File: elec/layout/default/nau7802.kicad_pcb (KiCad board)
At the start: 2 copper layers, 225.7 x 100.8 mm, 7 parts

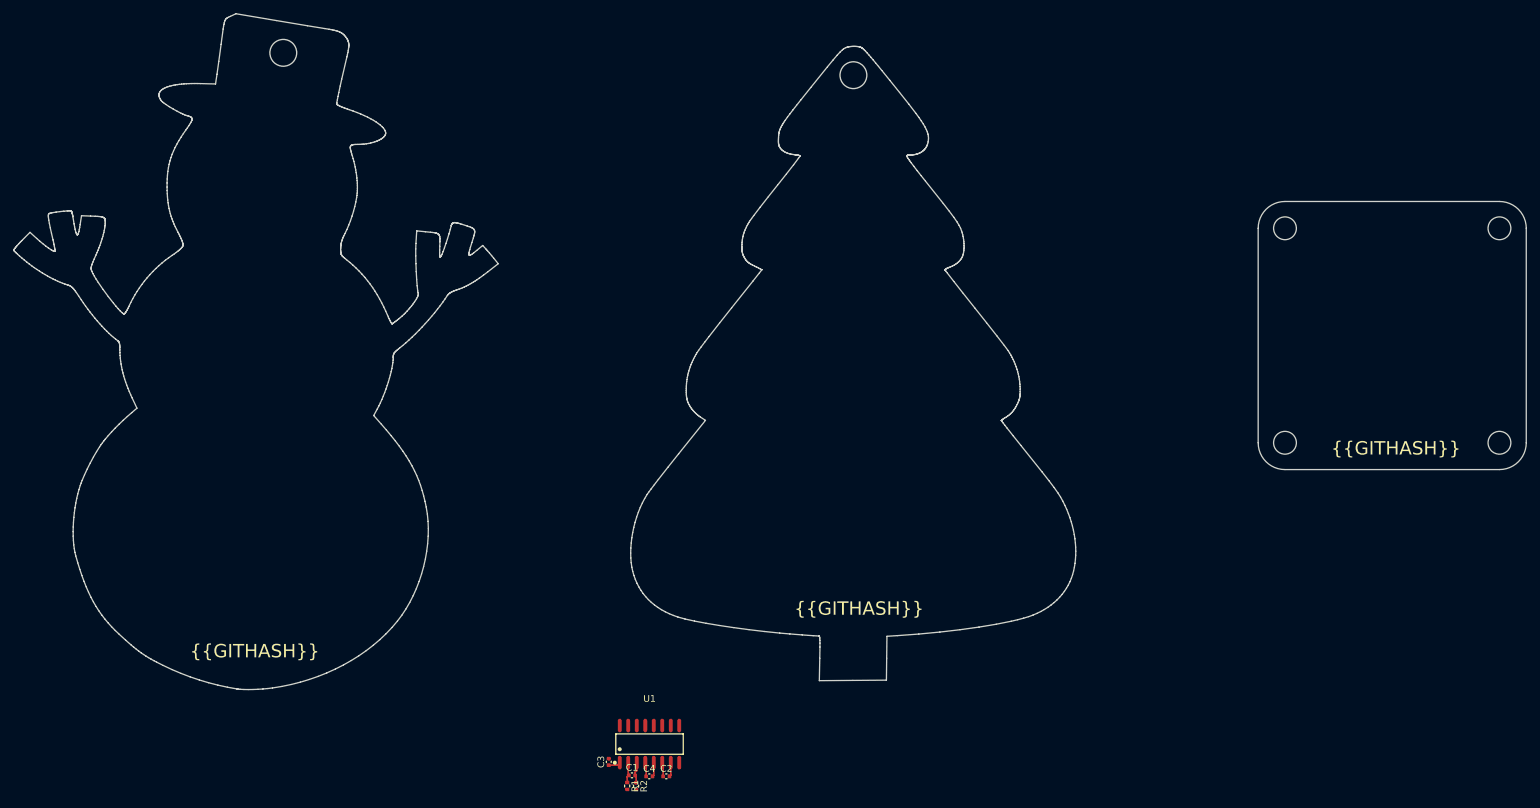
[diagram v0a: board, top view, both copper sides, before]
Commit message: Add dual sensor build
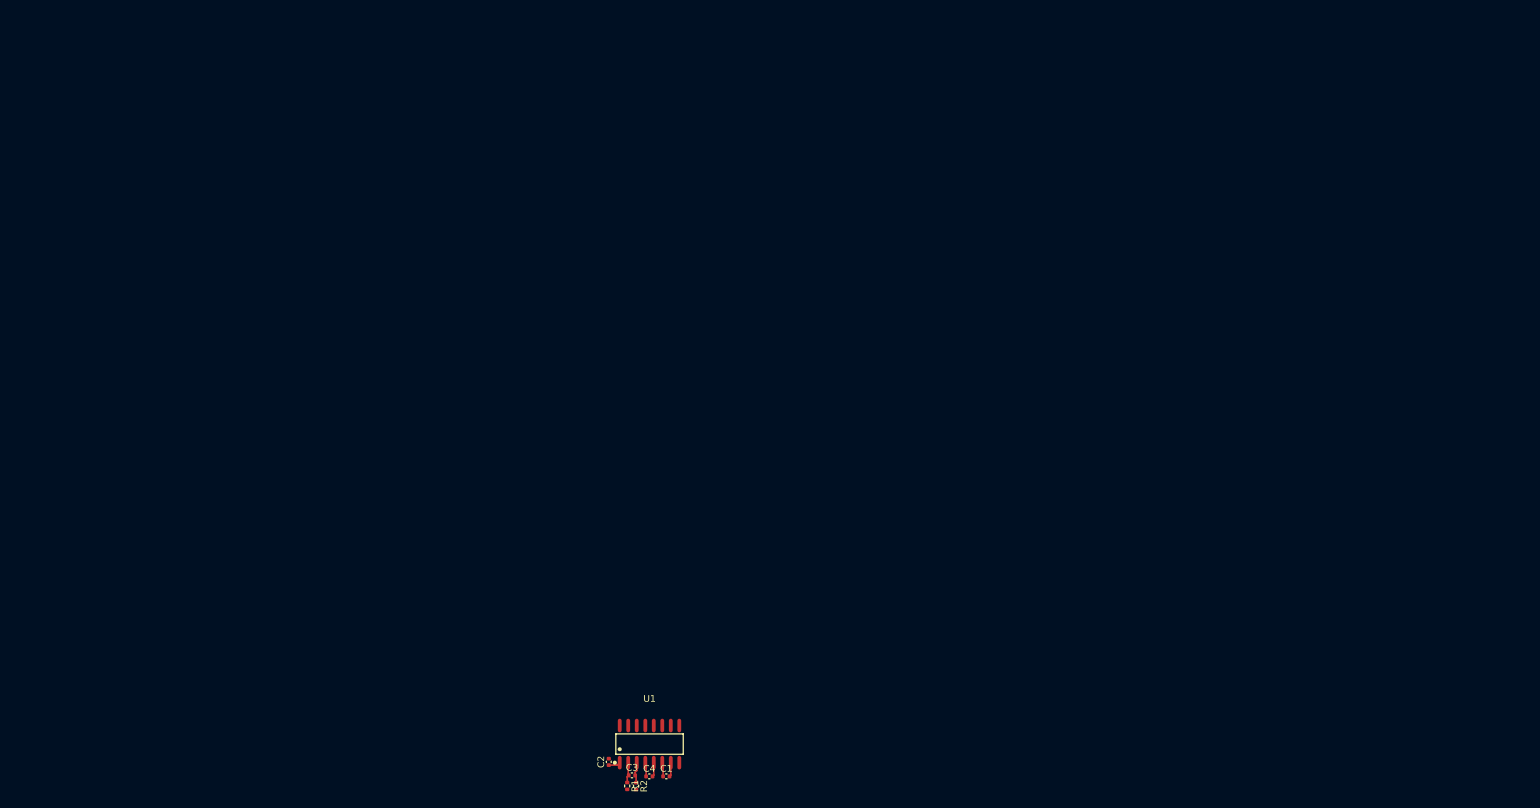
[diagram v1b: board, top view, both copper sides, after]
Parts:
- C1: renamed from C2; value Multilayer Ceramic Capacitors MLCC - SMD/SMT 100nF 10V 0402 RoHS -> 16V 100nF X7R ±10% 0402 Multilayer Ceramic Capacitors MLCC - SMD/SMT ROHS
- C2: renamed from C3; value Multilayer Ceramic Capacitors MLCC - SMD/SMT 100nF 10V 0402 RoHS -> 16V 100nF X7R ±10% 0402 Multilayer Ceramic Capacitors MLCC - SMD/SMT ROHS
- C3: renamed from C1; value Multilayer Ceramic Capacitors MLCC - SMD/SMT 100nF 10V 0402 RoHS -> 16V 100nF X7R ±10% 0402 Multilayer Ceramic Capacitors MLCC - SMD/SMT ROHS
- C4: value Multilayer Ceramic Capacitors MLCC - SMD/SMT 270pF 50V 0402 RoHS -> 50V 330pF X7R ±10% 0402 Multilayer Ceramic Capacitors MLCC - SMD/SMT ROHS
- R1, R2: value Chip Resistor - Surface Mount 51Ohms ±5% 1/16W 0402 RoHS -> 62.5mW Thick Film Resistors 50V ±100ppm/℃ ±1% 49.9Ω 0402 Chip Resistor - Surface Mount ROHS
- U1: value (none) -> ?
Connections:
- net dvdd renamed vcc
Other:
- board outline removed
- board text removed: "{{GITHASH}}"

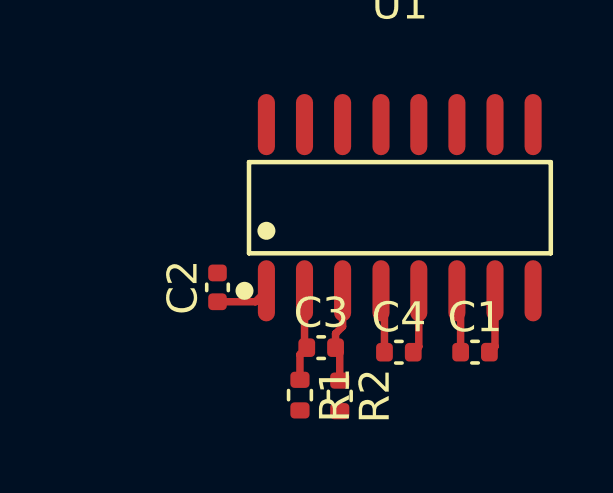
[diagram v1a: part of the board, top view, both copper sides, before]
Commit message: relink with 0.3 compiler
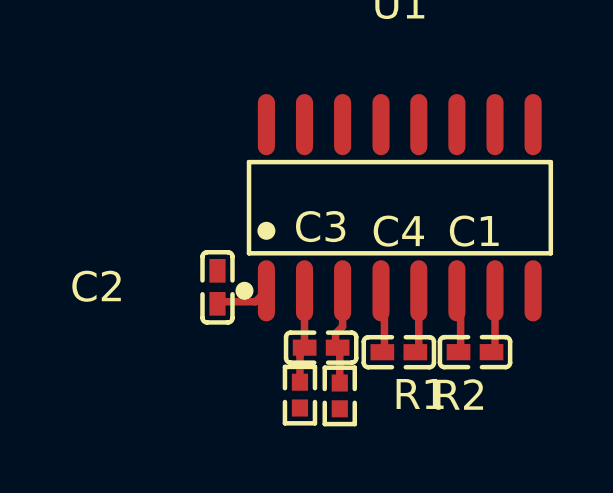
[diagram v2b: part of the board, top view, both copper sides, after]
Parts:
- C1, C2, C3: value 16V 100nF X7R ±10% 0402 Multilayer Ceramic Capacitors MLCC - SMD/SMT ROHS -> 100nF ±10% 16V X7R; footprint lib:C0402 -> atopile:C0402-b3ef17
- C4: value 50V 330pF X7R ±10% 0402 Multilayer Ceramic Capacitors MLCC - SMD/SMT ROHS -> 470pF ±10% 50V X7R; footprint lib:C0402 -> atopile:C0402-b3ef17
- R1, R2: value 62.5mW Thick Film Resistors 50V ±100ppm/℃ ±1% 49.9Ω 0402 Chip Resistor - Surface Mount ROHS -> 51Ω ±1% 62.5mW; footprint lib:R0402 -> atopile:R0402-56259e
- U1: value ? -> (none)
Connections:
- net avdd_ldo renamed AVDD_LDO
- net drdy renamed DRDY
- net refp renamed REFP
- net scl renamed SCL
- net sda renamed SDA
- net vbg renamed VBG
- net vcc renamed DVDD
- net vin1n renamed VIN1N
- net vin1p renamed VIN1P
- net vin2n renamed VIN2N
- net vin2p renamed VIN2P
- net xin renamed XIN
- net xout renamed XOUT
